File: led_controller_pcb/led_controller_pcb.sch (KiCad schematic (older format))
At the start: 1 part

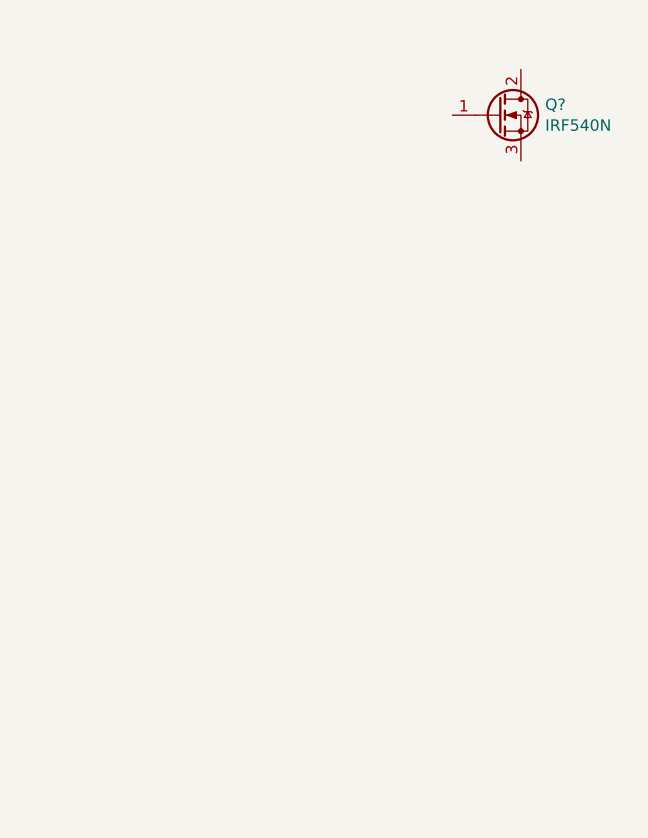
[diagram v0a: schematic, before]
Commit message: label mcu pins
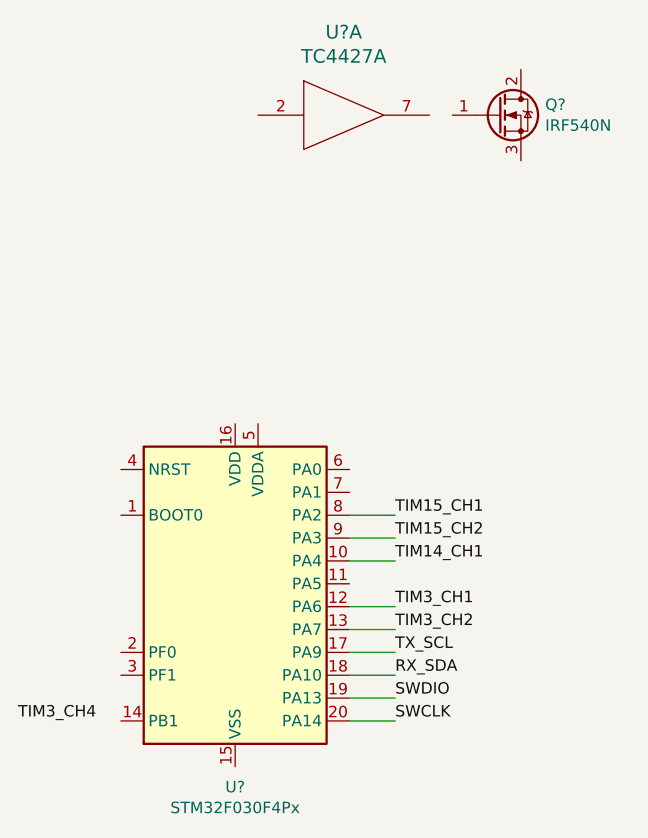
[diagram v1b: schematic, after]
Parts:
- added U?: TC4427A, symbol drivers_and_mosfets:TC4427A
- added U?: STM32F030F4Px, Package_SO:TSSOP-20_4.4x6.5mm_P0.65mm, symbol MCU_ST_STM32F0:STM32F030F4Px
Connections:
- new net GND: U?.3 (GND)
- new net RX_SDA: U?.18 (PA10)
- new net SWCLK: U?.20 (PA14)
- new net SWDIO: U?.19 (PA13)
- new net TIM14_CH1: U?.10 (PA4)
- new net TIM15_CH1: U?.8 (PA2)
- new net TIM15_CH2: U?.9 (PA3)
- new net TIM3_CH1: U?.12 (PA6)
- new net TIM3_CH2: U?.13 (PA7)
- new net TX_SCL: U?.17 (PA9)
- new net VDD: U?.6 (VDD)
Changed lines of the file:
@@
 	1    0    0    -1
 $EndComp
+$Comp
+L drivers_and_mosfets:TC4427A U?
+U 1 1 5D809F3E
+P 5850 2050
+F 0 "U?" H 5925 2413 60  0000 C CNN
+F 1 "TC4427A" H 5925 2307 60  0000 C CNN
+F 2 "" H 5800 2050 60  0001 C CNN
+F 3 "" H 5800 2050 60  0001 C CNN
+	1    5850 2050
+	1    0    0    -1
+$EndComp
+$Comp
+L MCU_ST_STM32F0:STM32F030F4Px U?
+U 1 1 5D80BF07
+P 5450 4100
+F 0 "U?" H 5450 3211 50  0000 C CNN
+F 1 "STM32F030F4Px" H 5450 3120 50  0000 C CNN
+F 2 "Package_SO:TSSOP-20_4.4x6.5mm_P0.65mm" H 5050 3400 50  0001 R CNN
+F 3 "http://www.st.com/st-web-ui/static/active/en/resource/technical/document/datasheet/DM00088500.pdf" H 5450 4100 50  0001 C CNN
+	1    5450 4100
+	1    0    0    -1
+$EndComp
+Wire Wire Line
+	5950 4600 6150 4600
+Text Label 6150 4600 0    50   ~ 0
+SWDIO
+Wire Wire Line
+	5950 4700 6150 4700
+Text Label 6150 4700 0    50   ~ 0
+SWCLK
+Text Label 6150 4200 0    50   ~ 0
+TIM3_CH1
+Text Label 6150 4300 0    50   ~ 0
+TIM3_CH2
+Text Label 6150 4000 0    50   ~ 0
+TIM14_CH1
+Text Label 6150 3800 0    50   ~ 0
+TIM15_CH1
+Text Label 6150 3900 0    50   ~ 0
+TIM15_CH2
+Text Label 4500 4700 0    50   ~ 0
+TIM3_CH4
+Wire Wire Line
+	5950 4400 6150 4400
+Wire Wire Line
+	5950 4500 6150 4500
+Text Label 6150 4400 0    50   ~ 0
+TX_SCL
+Text Label 6150 4500 0    50   ~ 0
+RX_SDA
+Wire Wire Line
+	6150 4300 5950 4300
+Wire Wire Line
+	5950 4200 6150 4200
+Wire Wire Line
+	6150 4000 5950 4000
+Wire Wire Line
+	5950 3900 6150 3900
+Wire Wire Line
+	6150 3800 5950 3800
 $EndSCHEMATC

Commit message: some more schematic work
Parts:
- added C? (x4): 100n, Capacitor_SMD:C_0805_2012Metric, symbol Device:C
- added C? (x2): 470uF, Capacitor_THT:CP_Radial_D8.0mm_P3.50mm, symbol Device:CP
- added C? (x2): 20pF, Capacitor_SMD:C_0805_2012Metric, symbol Device:C
- added D? (x3): LED, symbol Device:LED
- added D? (x2): 1N47xxA, Diode_THT:D_DO-41_SOD81_P10.16mm_Horizontal, symbol Diode:1N47xxA
- added J? (x2): HV_OUT, symbol Connector:Screw_Terminal_01x01
- added J? (x2): HV_LINE, symbol Connector:Screw_Terminal_01x01
- added J?: DCDC, symbol Connector_Generic:Conn_01x04
- added J? (x5): OUT, symbol Connector:Screw_Terminal_01x01
- added J?: VPP, symbol Connector:Screw_Terminal_01x01
- added J?: PSU_LINE1, symbol Connector:Screw_Terminal_01x01
- added J?: PSU_LINE2, symbol Connector:Screw_Terminal_01x01
- added J?: PSU_SHIELD, symbol Connector:Screw_Terminal_01x01
- added J?: PSU_GND, symbol Connector:Screw_Terminal_01x01
- added J?: PSU_VOUT, symbol Connector:Screw_Terminal_01x01
- added J?: LINE2_IN, symbol Connector:Screw_Terminal_01x01
- added J?: LINE1_IN, symbol Connector:Screw_Terminal_01x01
- added J?: DEBUG, symbol Connector_Generic:Conn_02x07_Counter_Clockwise
- added Q? (x5): IRF540N, Package_TO_SOT_THT:TO-220-3_Vertical, symbol Transistor_FET:IRF540N
- added Q? (x2): BT136-600, Package_TO_SOT_THT:TO-220-3_Vertical, symbol Triac_Thyristor:BT136-600
- added Q? (x2): BC549, Package_TO_SOT_THT:TO-92, symbol Transistor_BJT:BC549
- added R? (x6): 47k, symbol Device:R
- added R? (x4): 10k, symbol Device:R
- added R? (x8): 4.7k, symbol Device:R
- added R? (x2): R, symbol Device:R
- added R? (x2): 330, symbol Device:R
- added R? (x4): 1k, symbol Device:R
- added R?: LDR03, OptoDevice:R_LDR_10x8.5mm_P7.6mm_Vertical, symbol Sensor_Optical:LDR03
- added R?: 150k, symbol Device:R
- added SW? (x2): BUTTON, symbol Switch:SW_Push
- added U? (x5): TC4427A, symbol drivers_and_mosfets:TC4427A
- added U?: EL814, symbol Isolator:EL814
- added U? (x2): MOC3023M, symbol Relay_SolidState:MOC3023M
- added U?: ESP-12E, RF_Module:ESP-12E, symbol RF_Module:ESP-12E
- added Y?: 8MHz, Crystal:Crystal_HC49-U_Vertical, symbol Device:Crystal
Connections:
- net labels added: +3.3V, AC_SYNC, BOOT0, ESP_GP0, ESP_RST, ESP_RX, ESP_TX, GNDD, GPO1, GPO2, LINE1, LINE2, RST, VPP
- wire segments 9 -> 236
- no-connect marks 0 -> 8
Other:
- note added: "HIGH VOLTAGE"
- moved on the sheet: Q?, U?, U?A

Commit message: finalise schematic
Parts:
- removed J? (x2): OUT, symbol Connector:Screw_Terminal_01x01
- removed J?: DEBUG, symbol Connector_Generic:Conn_02x07_Counter_Clockwise
- added F1: Fuse, Fuse:Fuseholder_Cylinder-5x20mm_Stelvio-Kontek_PTF78_Horizontal_Open, symbol Device:Fuse
- added J10, J16, J4: PASSIVE_OUT, connectors:1PIN_DG306, symbol Connector:Screw_Terminal_01x01
- added J11, J13, J15, J17, J19, J3, J7, J9: VPP, connectors:1PIN_DG306, symbol Connector:Screw_Terminal_01x01
- added J14, J20, J8: OUT, connectors:1PIN_DG306, symbol Connector:Screw_Terminal_01x01
- added J2: DEBUG, Connector_PinHeader_2.54mm:PinHeader_2x07_P2.54mm_Vertical, symbol Connector_Generic:Conn_02x07_Odd_Even
- added J23: LINE_SHIELD, connectors:1PIN_DG306, symbol Connector:Screw_Terminal_01x01
- D1, D2, D3: renamed from D?; footprint (none) -> LED_THT:LED_D5.0mm
- J1: renamed from J?; footprint (none) -> Connector_PinHeader_2.54mm:PinHeader_1x04_P2.54mm_Vertical
- J12, J18, J21, J22, J24, J25, J26, J27, J28, J29, J30, J31, J32, J5, J6: renamed from J?; footprint (none) -> connectors:1PIN_DG306
- U2, U3, U4: renamed from U?; footprint (none) -> Package_SO:SOIC-8_3.9x4.9mm_P1.27mm
- gave numbers to parts that had none: 56
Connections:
- net labels added: GND, VDD
- net labels removed: GNDD, VPP
- wire segments 236 -> 250
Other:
- moved on the sheet: C5, C7, C8, D4, D5, J12, J18, J21, J22, J24, J25, J26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

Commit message: pcb taking shape
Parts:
- removed D3: LED, LED_THT:LED_D5.0mm, symbol Device:LED
- removed F1: Fuse, Fuse:Fuseholder_Cylinder-5x20mm_Stelvio-Kontek_PTF78_Horizontal_Open, symbol Device:Fuse
- removed J23: LINE_SHIELD, connectors:1PIN_DG306, symbol Connector:Screw_Terminal_01x01
- removed J30: PSU_SHIELD, connectors:1PIN_DG306, symbol Connector:Screw_Terminal_01x01
- removed R17: 4.7k, symbol Device:R
- removed U8: EL814, symbol Isolator:EL814
- added U8: H11AA1, Package_DIP:DIP-6_W7.62mm, symbol Isolator:H11AA1
- R1: footprint OptoDevice:R_LDR_10x8.5mm_P7.6mm_Vertical -> Connector_PinHeader_2.54mm:PinHeader_1x02_P2.54mm_Vertical
- R10, R11, R12, R13, R14, R15, R16, R18, R19, R2, R20, R21, R22, R23, R28, R3, R4, R5, R6, R7, R8, R9: footprint (none) -> Resistor_SMD:R_0805_2012Metric
- R24, R25, R26, R27: footprint (none) -> Resistor_THT:R_Axial_DIN0207_L6.3mm_D2.5mm_P10.16mm_Horizontal
- SW1, SW2: footprint (none) -> Connector_PinHeader_2.54mm:PinHeader_1x02_P2.54mm_Vertical
- U6, U7: footprint (none) -> Package_DIP:DIP-6_W7.62mm
- Y1: footprint Crystal:Crystal_HC49-U_Vertical -> Crystal:Crystal_SMD_HC49-SD
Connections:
- wire segments 250 -> 245
- no-connect marks 8 -> 9

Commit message: pcb all connected
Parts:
- removed D1: LED, LED_THT:LED_D5.0mm, symbol Device:LED
- removed R5: 4.7k, Resistor_SMD:R_0805_2012Metric, symbol Device:R
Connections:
- wire segments 245 -> 241
- no-connect marks 9 -> 10
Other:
- moved on the sheet: D2, R11, R12, R6
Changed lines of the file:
@@
 L Device:R R11
 U 1 1 5D855C26
-P 6350 4700
-F 0 "R11" H 6420 4746 50  0000 L CNN
-F 1 "47k" H 6420 4655 50  0000 L CNN
-F 2 "Resistor_SMD:R_0805_2012Metric" V 6280 4700 50  0001 C CNN
-F 3 "~" H 6350 4700 50  0001 C CNN
-	1    6350 4700
+P 6350 6450
+F 0 "R11" H 6420 6496 50  0000 L CNN
+F 1 "47k" H 6420 6405 50  0000 L CNN
+F 2 "Resistor_SMD:R_0805_2012Metric" V 6280 6450 50  0001 C CNN
+F 3 "~" H 6350 6450 50  0001 C CNN
+	1    6350 6450
 	1    0    0    -1
 $EndComp
@@
 L Device:R R12
 U 1 1 5D865B5F
-P 6350 6450
-F 0 "R12" H 6420 6496 50  0000 L CNN
-F 1 "47k" H 6420 6405 50  0000 L CNN
-F 2 "Resistor_SMD:R_0805_2012Metric" V 6280 6450 50  0001 C CNN
-F 3 "~" H 6350 6450 50  0001 C CNN
-	1    6350 6450
+P 6350 4700
+F 0 "R12" H 6420 4746 50  0000 L CNN
+F 1 "47k" H 6420 4655 50  0000 L CNN
+F 2 "Resistor_SMD:R_0805_2012Metric" V 6280 4700 50  0001 C CNN
+F 3 "~" H 6350 4700 50  0001 C CNN
+	1    6350 4700
 	1    0    0    -1
 $EndComp
@@
 Wire Wire Line
 	8700 6250 8600 6250
-Text Label 5900 4500 0    50   ~ 0
+Text Label 5900 6250 0    50   ~ 0
 TIM15_CH2
 Text Label 8150 4500 0    50   ~ 0
@@
 Text Label 3700 6250 0    50   ~ 0
 TIM3_CH1
-Text Label 5900 6250 0    50   ~ 0
+Text Label 5900 4500 0    50   ~ 0
 TIM3_CH2
 Text Label 8150 6250 0    50   ~ 0
@@
 Wire Wire Line
 	2350 8650 2350 9050
-NoConn ~ 4450 9600
 NoConn ~ 4450 9500
 NoConn ~ 4450 9400
@@
 L Device:LED D2
 U 1 1 5D84BC31
-P 2800 10150
-F 0 "D2" V 2900 10150 50  0000 R CNN
-F 1 "LED" V 2748 10033 50  0001 R CNN
-F 2 "LED_THT:LED_D5.0mm" H 2800 10150 50  0001 C CNN
-F 3 "~" H 2800 10150 50  0001 C CNN
-	1    2800 10150
+P 4600 10850
+F 0 "D2" V 4700 10850 50  0000 R CNN
+F 1 "LED" V 4548 10733 50  0001 R CNN
+F 2 "LED_THT:LED_D5.0mm" H 4600 10850 50  0001 C CNN
+F 3 "~" H 4600 10850 50  0001 C CNN
+	1    4600 10850
 	0    -1   -1   0
 $EndComp
-$Comp
-L Device:R R5
-U 1 1 5D84D6AC
-P 3000 9800
-F 0 "R5" V 2950 9600 50  0000 C CNN
-F 1 "4.7k" V 3000 9800 50  0000 C CNN
-F 2 "Resistor_SMD:R_0805_2012Metric" V 2930 9800 50  0001 C CNN
-F 3 "~" H 3000 9800 50  0001 C CNN
-	1    3000 9800
-	0    1    1    0
-$EndComp
-$Comp
-L Device:R R6
-U 1 1 5D84DAC4
-P 3000 9900
-F 0 "R6" V 2950 9700 50  0000 C CNN
-F 1 "4.7k" V 3000 9900 50  0000 C CNN
-F 2 "Resistor_SMD:R_0805_2012Metric" V 2930 9900 50  0001 C CNN
-F 3 "~" H 3000 9900 50  0001 C CNN
-	1    3000 9900
-	0    1    1    0
-$EndComp
-$Comp
-L Device:LED D1
-U 1 1 5D84E6AC
-P 2550 10150
-F 0 "D1" V 2650 10050 50  0000 L CNN
-F 1 "LED" V 2498 10033 50  0001 R CNN
-F 2 "LED_THT:LED_D5.0mm" H 2550 10150 50  0001 C CNN
-F 3 "~" H 2550 10150 50  0001 C CNN
-	1    2550 10150
-	0    -1   -1   0
-$EndComp
-Wire Wire Line
-	2800 10000 2800 9900
-Wire Wire Line
-	2800 9900 2850 9900
-Wire Wire Line
-	2850 9800 2550 9800
-Wire Wire Line
-	2550 9800 2550 10000
-$Comp
-L power:GND #PWR012
-U 1 1 5D84F0A3
-P 2550 10400
-F 0 "#PWR012" H 2550 10150 50  0001 C CNN
-F 1 "GND" H 2554 10245 50  0001 C CNN
-F 2 "" H 2550 10400 50  0001 C CNN
-F 3 "" H 2550 10400 50  0001 C CNN
-	1    2550 10400
-	1    0    0    -1
-$EndComp
+Wire Wire Line
+	4600 10700 4600 10600
 $Comp
 L power:GND #PWR014
 U 1 1 5D84F320
-P 2800 10400
-F 0 "#PWR014" H 2800 10150 50  0001 C CNN
-F 1 "GND" H 2804 10245 50  0001 C CNN
-F 2 "" H 2800 10400 50  0001 C CNN
-F 3 "" H 2800 10400 50  0001 C CNN
-	1    2800 10400
-	1    0    0    -1
-$EndComp
-Wire Wire Line
-	2800 10400 2800 10300
-Wire Wire Line
-	2550 10400 2550 10300
-Wire Wire Line
-	3150 9800 3250 9800
-Wire Wire Line
-	3250 9900 3150 9900
+P 4600 11100
+F 0 "#PWR014" H 4600 10850 50  0001 C CNN
+F 1 "GND" H 4604 10945 50  0001 C CNN
+F 2 "" H 4600 11100 50  0001 C CNN
+F 3 "" H 4600 11100 50  0001 C CNN
+	1    4600 11100
+	1    0    0    -1
+$EndComp
+Wire Wire Line
+	4600 11100 4600 11000
 $Comp
 L Device:Crystal Y1
@@
 Text Label 12750 7650 0    50   ~ 0
 LINE1
+$Comp
+L Device:R R6
+U 1 1 5D84DAC4
+P 4600 10450
+F 0 "R6" V 4550 10250 50  0000 C CNN
+F 1 "4.7k" V 4600 10450 50  0000 C CNN
+F 2 "Resistor_SMD:R_0805_2012Metric" V 4530 10450 50  0001 C CNN
+F 3 "~" H 4600 10450 50  0001 C CNN
+	1    4600 10450
+	-1   0    0    1
+$EndComp
+Wire Wire Line
+	4600 10300 4600 9600
+Wire Wire Line
+	4600 9600 4450 9600
+NoConn ~ 3250 9800
+NoConn ~ 3250 9900
 $EndSCHEMATC

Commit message: finish pcb
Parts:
- added C9: 100n, Capacitor_SMD:C_0805_2012Metric, symbol Device:C
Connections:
- wire segments 241 -> 243
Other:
- moved on the sheet: D4, D5, R26, R27
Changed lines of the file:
@@
 L Diode:1N47xxA D4
 U 1 1 5D90091E
+P 14500 5900
+F 0 "D4" V 14500 5979 50  0000 L CNN
+F 1 "1N47xxA" V 14550 6050 50  0001 L CNN
+F 2 "Diode_THT:D_DO-41_SOD81_P10.16mm_Horizontal" H 14500 5725 50  0001 C CNN
+F 3 "https://www.vishay.com/docs/85816/1n4728a.pdf" H 14500 5900 50  0001 C CNN
+	1    14500 5900
+	0    1    -1   0
+$EndComp
+$Comp
+L Diode:1N47xxA D5
+U 1 1 5D90F23F
 P 14500 5500
-F 0 "D4" V 14500 5579 50  0000 L CNN
+F 0 "D5" V 14500 5578 50  0000 L CNN
 F 1 "1N47xxA" V 14550 5650 50  0001 L CNN
 F 2 "Diode_THT:D_DO-41_SOD81_P10.16mm_Horizontal" H 14500 5325 50  0001 C CNN
 F 3 "https://www.vishay.com/docs/85816/1n4728a.pdf" H 14500 5500 50  0001 C CNN
 	1    14500 5500
-	0    1    1    0
-$EndComp
-$Comp
-L Diode:1N47xxA D5
-U 1 1 5D90F23F
-P 14500 5900
-F 0 "D5" V 14500 5978 50  0000 L CNN
-F 1 "1N47xxA" V 14550 6050 50  0001 L CNN
-F 2 "Diode_THT:D_DO-41_SOD81_P10.16mm_Horizontal" H 14500 5725 50  0001 C CNN
-F 3 "https://www.vishay.com/docs/85816/1n4728a.pdf" H 14500 5900 50  0001 C CNN
-	1    14500 5900
-	0    -1   -1   0
-$EndComp
-Wire Wire Line
-	14500 5650 14500 5750
+	0    -1   1    0
+$EndComp
+Wire Wire Line
+	14500 5750 14500 5650
+Wire Wire Line
+	14300 6100 14500 6100
+Wire Wire Line
+	14800 5300 14800 5600
+Wire Wire Line
+	14800 5600 14900 5600
 Wire Wire Line
 	14300 5300 14500 5300
 Wire Wire Line
-	14800 5300 14800 5600
-Wire Wire Line
-	14800 5600 14900 5600
-Wire Wire Line
-	14300 6100 14500 6100
-Wire Wire Line
 	14800 6100 14800 5800
 Wire Wire Line
 	14800 5800 14900 5800
+Wire Wire Line
+	14500 5350 14500 5300
+Connection ~ 14500 5300
+Wire Wire Line
+	14500 5300 14800 5300
 Wire Wire Line
 	14500 6050 14500 6100
@@
 	14500 6100 14800 6100
 Wire Wire Line
-	14500 5350 14500 5300
-Connection ~ 14500 5300
-Wire Wire Line
-	14500 5300 14800 5300
+	14000 6100 13750 6100
 Wire Wire Line
 	14000 5300 13750 5300
-Wire Wire Line
-	14000 6100 13750 6100
+Text Label 13750 6100 0    50   ~ 0
+LINE1
 Text Label 13750 5300 0    50   ~ 0
-LINE1
-Text Label 13750 6100 0    50   ~ 0
 LINE2
 $Comp
@@
 L Device:R R27
 U 1 1 5D91DE87
+P 14150 5300
+F 0 "R27" V 13943 5300 50  0000 C CNN
+F 1 "R" V 14034 5300 50  0000 C CNN
+F 2 "Resistor_THT:R_Axial_DIN0207_L6.3mm_D2.5mm_P10.16mm_Horizontal" V 14080 5300 50  0001 C CNN
+F 3 "~" H 14150 5300 50  0001 C CNN
+	1    14150 5300
+	0    1    -1   0
+$EndComp
+$Comp
+L Device:R R26
+U 1 1 5D903AAF
 P 14150 6100
-F 0 "R27" V 13943 6100 50  0000 C CNN
+F 0 "R26" V 13943 6100 50  0000 C CNN
 F 1 "R" V 14034 6100 50  0000 C CNN
 F 2 "Resistor_THT:R_Axial_DIN0207_L6.3mm_D2.5mm_P10.16mm_Horizontal" V 14080 6100 50  0001 C CNN
 F 3 "~" H 14150 6100 50  0001 C CNN
 	1    14150 6100
-	0    1    1    0
-$EndComp
-$Comp
-L Device:R R26
-U 1 1 5D903AAF
-P 14150 5300
-F 0 "R26" V 13943 5300 50  0000 C CNN
-F 1 "R" V 14034 5300 50  0000 C CNN
-F 2 "Resistor_THT:R_Axial_DIN0207_L6.3mm_D2.5mm_P10.16mm_Horizontal" V 14080 5300 50  0001 C CNN
-F 3 "~" H 14150 5300 50  0001 C CNN
-	1    14150 5300
-	0    1    1    0
+	0    1    -1   0
 $EndComp
 $Comp
@@
 NoConn ~ 3250 9800
 NoConn ~ 3250 9900
+$Comp
+L power:GND #PWR0114
+U 1 1 5DA90CAE
+P 1550 6200
+F 0 "#PWR0114" H 1550 5950 50  0001 C CNN
+F 1 "GND" H 1554 6045 50  0001 C CNN
+F 2 "" H 1550 6200 50  0001 C CNN
+F 3 "" H 1550 6200 50  0001 C CNN
+	1    1550 6200
+	1    0    0    -1
+$EndComp
+Wire Wire Line
+	1550 6200 1550 6100
+Wire Wire Line
+	1550 5800 1550 5700
+$Comp
+L Device:C C9
+U 1 1 5DA90CBE
+P 1550 5950
+F 0 "C9" H 1665 5996 50  0000 L CNN
+F 1 "100n" H 1665 5905 50  0000 L CNN
+F 2 "Capacitor_SMD:C_0805_2012Metric" H 1588 5800 50  0001 C CNN
+F 3 "~" H 1550 5950 50  0001 C CNN
+	1    1550 5950
+	1    0    0    -1
+$EndComp
+$Comp
+L power:+3.3V #PWR0115
+U 1 1 5DA90CCB
+P 1550 5700
+F 0 "#PWR0115" H 1550 5550 50  0001 C CNN
+F 1 "+3.3V" H 1565 5873 50  0000 C CNN
+F 2 "" H 1550 5700 50  0001 C CNN
+F 3 "" H 1550 5700 50  0001 C CNN
+	1    1550 5700
+	1    0    0    -1
+$EndComp
 $EndSCHEMATC

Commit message: the battle against TIM1 goes strong
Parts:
- U6, U7: symbol Relay_SolidState:MOC3023M -> led_controller_pcb-rescue:MOC3023M-Relay_SolidState
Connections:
- net labels added: RX, TIM1_CH2, TIM1_CH3, TX
- net labels removed: RX_SDA, TIM15_CH1, TIM15_CH2, TX_SCL
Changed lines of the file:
@@
 Text Label 9950 9200 0    50   ~ 0
 TIM14_CH1
-Text Label 9950 9000 0    50   ~ 0
-TIM15_CH1
-Text Label 9950 9100 0    50   ~ 0
-TIM15_CH2
 Text Label 8300 9900 0    50   ~ 0
 TIM3_CH4
@@
 Wire Wire Line
 	9750 9700 9950 9700
-Text Label 9950 9600 0    50   ~ 0
-TX_SCL
-Text Label 9950 9700 0    50   ~ 0
-RX_SDA
+Text Label 9950 9000 0    50   ~ 0
+TX
+Text Label 9950 9100 0    50   ~ 0
+RX
 Wire Wire Line
 	9950 9500 9750 9500
@@
 	4250 4500 4150 4500
 Text Label 3700 4500 0    50   ~ 0
-TIM15_CH1
+TIM1_CH2
 $Comp
 L Device:R R7
@@
 	8700 6250 8600 6250
 Text Label 5900 6250 0    50   ~ 0
-TIM15_CH2
+TIM1_CH3
 Text Label 8150 4500 0    50   ~ 0
 TIM14_CH1
@@
 	14000 2150 13550 2150
 $Comp
-L Relay_SolidState:MOC3023M U6
+L led_controller_pcb-rescue:MOC3023M-Relay_SolidState U6
 U 1 1 5D957503
 P 13250 2050
@@
 	14150 4400 14400 4400
 $Comp
-L Relay_SolidState:MOC3023M U7
+L led_controller_pcb-rescue:MOC3023M-Relay_SolidState U7
 U 1 1 5DA06959
 P 13250 4100
@@
 	5500 9200 5650 9200
 Text Label 5650 9100 0    50   ~ 0
-RX_SDA
+RX
 Text Label 5650 9200 0    50   ~ 0
-TX_SCL
+TX
 Text Label 5650 9000 0    50   ~ 0
 SWDIO
@@
 	1    0    0    -1
 $EndComp
+Text Label 9950 9600 0    50   ~ 0
+TIM1_CH2
+Text Label 9950 9700 0    50   ~ 0
+TIM1_CH3
 $EndSCHEMATC

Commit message: finalise PCB
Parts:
- added C10: 10p, Capacitor_SMD:C_0805_2012Metric, symbol Device:C
- added R?: 4.7k, Resistor_SMD:R_0805_2012Metric, symbol Device:R
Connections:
- wire segments 243 -> 249
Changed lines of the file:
@@
 	4800 9400 5000 9400
 Wire Wire Line
-	4450 9000 5000 9000
+	4450 9000 4550 9000
 Wire Wire Line
 	8750 9000 8550 9000
@@
 Text Label 4650 9000 0    50   ~ 0
 ESP_GP0
-Text Label 4350 8700 0    50   ~ 0
+Text Label 4100 8700 0    50   ~ 0
 ESP_RST
 Text Label 5650 9400 0    50   ~ 0
@@
 	5000 8800 4900 8800
 Wire Wire Line
-	4900 8800 4900 8650
+	4900 8800 4900 8100
 Wire Wire Line
 	5500 8800 6150 8800
@@
 F 3 "" H 6150 8900 50  0001 C CNN
 	1    6150 8900
-	1    0    0    -1
-$EndComp
-$Comp
-L power:+3.3V #PWR019
-U 1 1 5DB7A1AD
-P 4900 8650
-F 0 "#PWR019" H 4900 8500 50  0001 C CNN
-F 1 "+3.3V" H 4915 8823 50  0000 C CNN
-F 2 "" H 4900 8650 50  0001 C CNN
-F 3 "" H 4900 8650 50  0001 C CNN
-	1    4900 8650
 	1    0    0    -1
 $EndComp
@@
 $EndComp
 Wire Wire Line
-	3250 9400 2350 9400
+	3250 9400 2700 9400
 Wire Wire Line
 	2350 9400 2350 9350
@@
 Text Label 9950 9700 0    50   ~ 0
 TIM1_CH3
+Wire Wire Line
+	2700 9500 2700 9400
+$Comp
+L Device:C C10
+U 1 1 5D98DECE
+P 2700 9650
+F 0 "C10" H 2815 9696 50  0000 L CNN
+F 1 "10p" H 2815 9605 50  0000 L CNN
+F 2 "Capacitor_SMD:C_0805_2012Metric" H 2738 9500 50  0001 C CNN
+F 3 "~" H 2700 9650 50  0001 C CNN
+	1    2700 9650
+	1    0    0    -1
+$EndComp
+$Comp
+L power:GND #PWR0116
+U 1 1 5D98DEDB
+P 2700 10400
+F 0 "#PWR0116" H 2700 10150 50  0001 C CNN
+F 1 "GND" H 2704 10245 50  0001 C CNN
+F 2 "" H 2700 10400 50  0001 C CNN
+F 3 "" H 2700 10400 50  0001 C CNN
+	1    2700 10400
+	1    0    0    -1
+$EndComp
+Wire Wire Line
+	2700 10400 2700 9800
+Connection ~ 2700 9400
+Wire Wire Line
+	2700 9400 2350 9400
+$Comp
+L Device:R R?
+U 1 1 5D9DC575
+P 4550 8400
+F 0 "R?" V 4450 8400 50  0000 C CNN
+F 1 "4.7k" V 4550 8400 50  0000 C CNN
+F 2 "Resistor_SMD:R_0805_2012Metric" V 4480 8400 50  0001 C CNN
+F 3 "~" H 4550 8400 50  0001 C CNN
+	1    4550 8400
+	-1   0    0    1
+$EndComp
+Wire Wire Line
+	4550 8550 4550 9000
+Connection ~ 4550 9000
+Wire Wire Line
+	4550 9000 5000 9000
+$Comp
+L power:+3.3V #PWR019
+U 1 1 5DB7A1AD
+P 4900 8100
+F 0 "#PWR019" H 4900 7950 50  0001 C CNN
+F 1 "+3.3V" H 4915 8273 50  0000 C CNN
+F 2 "" H 4900 8100 50  0001 C CNN
+F 3 "" H 4900 8100 50  0001 C CNN
+	1    4900 8100
+	1    0    0    -1
+$EndComp
+$Comp
+L power:+3.3V #PWR?
+U 1 1 5D9DED9E
+P 4550 8100
+F 0 "#PWR?" H 4550 7950 50  0001 C CNN
+F 1 "+3.3V" H 4565 8273 50  0000 C CNN
+F 2 "" H 4550 8100 50  0001 C CNN
+F 3 "" H 4550 8100 50  0001 C CNN
+	1    4550 8100
+	1    0    0    -1
+$EndComp
+Wire Wire Line
+	4550 8100 4550 8250
 $EndSCHEMATC
